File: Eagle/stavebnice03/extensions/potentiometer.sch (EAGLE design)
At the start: 4 parts

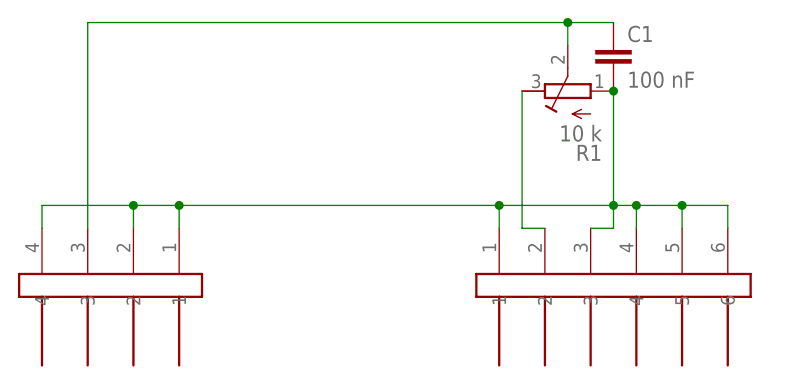
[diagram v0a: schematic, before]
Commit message: eagle adjustment for the Jíťa version
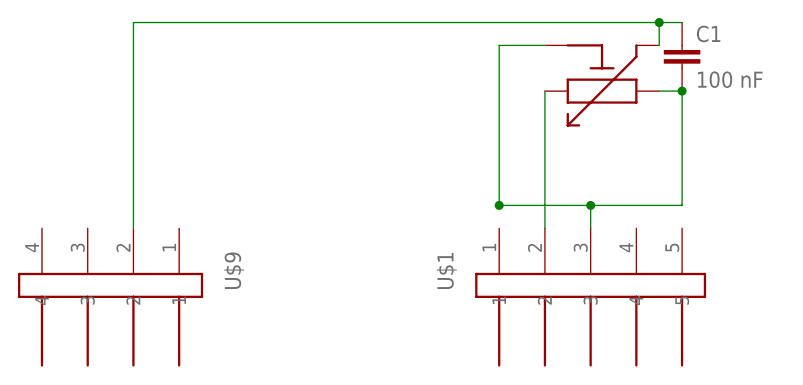
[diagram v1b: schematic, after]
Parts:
- removed R1: 10 k, !stavebnice03:R-TRIM
- removed U$8: JUMPER6M, !stavebnice03:JUMPER6M
- added U$1: JUMPER5M, !stavebnice03:JUMPER5M
- added U$2: POTENTIOMETER-RK09, !stavebnice03:POTENTIOMETER-RK09
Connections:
- net GND: now also U$1.3, U$2.1, U$2.GND; no longer R1.E, U$8.1, U$8.3, U$8.4, U$8.5, U$8.6, U$9.1, U$9.2, U$9.4
- net N$1: now also U$2.2, U$9.2; no longer R1.S, U$9.3
- net N$2: now also U$1.2, U$2.3; no longer R1.A, U$8.2
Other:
- moved on the sheet: C1
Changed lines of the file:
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@@
 </classes>
 <parts>
-<part name="U$8" library="!stavebnice03" deviceset="JUMPER6M" device=""/>
 <part name="U$9" library="!stavebnice03" deviceset="JUMPER4M" device=""/>
-<part name="R1" library="!stavebnice03" deviceset="R-TRIM" device="" value="10 k"/>
 <part name="C1" library="resistor" deviceset="C-EU" device="C0805" value="100 nF"/>
+<part name="U$1" library="!stavebnice03" deviceset="JUMPER5M" device=""/>
+<part name="U$2" library="!stavebnice03" deviceset="POTENTIOMETER-RK09" device=""/>
 </parts>
 <sheets>
@@
 </plain>
 <instances>
-<instance part="U$8" gate="G$1" x="175.26" y="35.56" rot="MR270"/>
 <instance part="U$9" gate="G$1" x="119.38" y="35.56" rot="R270"/>
-<instance part="R1" gate="G$1" x="170.18" y="58.42" rot="R90"/>
-<instance part="C1" gate="G$1" x="175.26" y="63.5"/>
+<instance part="C1" gate="G$1" x="182.88" y="63.5"/>
+<instance part="U$1" gate="G$1" x="172.72" y="35.56" rot="MR270"/>
+<instance part="U$2" gate="G$1" x="177.8" y="58.42" rot="R180"/>
 </instances>
 <busses>
@@
 <net name="N$1" class="0">
 <segment>
-<pinref part="U$9" gate="G$1" pin="3"/>
-<wire x1="116.84" y1="43.18" x2="116.84" y2="66.04" width="0.1524" layer="91"/>
-<wire x1="116.84" y1="66.04" x2="170.18" y2="66.04" width="0.1524" layer="91"/>
-<wire x1="170.18" y1="66.04" x2="170.18" y2="63.5" width="0.1524" layer="91"/>
-<pinref part="R1" gate="G$1" pin="S"/>
+<wire x1="121.92" y1="66.04" x2="180.34" y2="66.04" width="0.1524" layer="91"/>
+<wire x1="180.34" y1="66.04" x2="180.34" y2="63.5" width="0.1524" layer="91"/>
 <pinref part="C1" gate="G$1" pin="1"/>
-<wire x1="170.18" y1="66.04" x2="175.26" y2="66.04" width="0.1524" layer="91"/>
-<junction x="170.18" y="66.04"/>
+<wire x1="180.34" y1="66.04" x2="182.88" y2="66.04" width="0.1524" layer="91"/>
+<junction x="180.34" y="66.04"/>
+<pinref part="U$2" gate="G$1" pin="2"/>
+<pinref part="U$9" gate="G$1" pin="2"/>
+<wire x1="121.92" y1="66.04" x2="121.92" y2="43.18" width="0.1524" layer="91"/>
 </segment>
 </net>
 <net name="N$2" class="0">
 <segment>
-<pinref part="U$8" gate="G$1" pin="2"/>
-<wire x1="167.64" y1="43.18" x2="165.1" y2="43.18" width="0.1524" layer="91"/>
-<pinref part="R1" gate="G$1" pin="A"/>
-<wire x1="165.1" y1="43.18" x2="165.1" y2="58.42" width="0.1524" layer="91"/>
+<wire x1="167.64" y1="43.18" x2="167.64" y2="58.42" width="0.1524" layer="91"/>
+<pinref part="U$2" gate="G$1" pin="3"/>
+<pinref part="U$1" gate="G$1" pin="2"/>
 </segment>
 </net>
 <net name="GND" class="0">
 <segment>
-<pinref part="U$8" gate="G$1" pin="3"/>
-<pinref part="R1" gate="G$1" pin="E"/>
-<wire x1="175.26" y1="43.18" x2="175.26" y2="45.72" width="0.1524" layer="91"/>
-<wire x1="175.26" y1="45.72" x2="175.26" y2="58.42" width="0.1524" layer="91"/>
-<wire x1="175.26" y1="43.18" x2="172.72" y2="43.18" width="0.1524" layer="91"/>
+<wire x1="172.72" y1="43.18" x2="172.72" y2="45.72" width="0.1524" layer="91"/>
+<wire x1="182.88" y1="45.72" x2="182.88" y2="58.42" width="0.1524" layer="91"/>
 <pinref part="C1" gate="G$1" pin="2"/>
-<junction x="175.26" y="58.42"/>
-<pinref part="U$9" gate="G$1" pin="1"/>
-<wire x1="127" y1="43.18" x2="127" y2="45.72" width="0.1524" layer="91"/>
-<pinref part="U$9" gate="G$1" pin="2"/>
-<wire x1="121.92" y1="43.18" x2="121.92" y2="45.72" width="0.1524" layer="91"/>
-<wire x1="121.92" y1="45.72" x2="111.76" y2="45.72" width="0.1524" layer="91"/>
-<pinref part="U$9" gate="G$1" pin="4"/>
-<wire x1="111.76" y1="43.18" x2="111.76" y2="45.72" width="0.1524" layer="91"/>
-<wire x1="121.92" y1="45.72" x2="127" y2="45.72" width="0.1524" layer="91"/>
-<junction x="121.92" y="45.72"/>
-<junction x="127" y="45.72"/>
-<wire x1="127" y1="45.72" x2="162.56" y2="45.72" width="0.1524" layer="91"/>
-<junction x="175.26" y="45.72"/>
-<pinref part="U$8" gate="G$1" pin="1"/>
-<wire x1="162.56" y1="45.72" x2="175.26" y2="45.72" width="0.1524" layer="91"/>
-<wire x1="162.56" y1="43.18" x2="162.56" y2="45.72" width="0.1524" layer="91"/>
-<pinref part="U$8" gate="G$1" pin="4"/>
-<wire x1="177.8" y1="43.18" x2="177.8" y2="45.72" width="0.1524" layer="91"/>
-<wire x1="177.8" y1="45.72" x2="175.26" y2="45.72" width="0.1524" layer="91"/>
-<pinref part="U$8" gate="G$1" pin="5"/>
-<wire x1="182.88" y1="43.18" x2="182.88" y2="45.72" width="0.1524" layer="91"/>
-<wire x1="182.88" y1="45.72" x2="177.8" y2="45.72" width="0.1524" layer="91"/>
-<wire x1="182.88" y1="45.72" x2="187.96" y2="45.72" width="0.1524" layer="91"/>
-<pinref part="U$8" gate="G$1" pin="6"/>
-<wire x1="187.96" y1="45.72" x2="187.96" y2="43.18" width="0.1524" layer="91"/>
-<junction x="177.8" y="45.72"/>
+<wire x1="162.56" y1="45.72" x2="172.72" y2="45.72" width="0.1524" layer="91"/>
+<wire x1="172.72" y1="45.72" x2="182.88" y2="45.72" width="0.1524" layer="91"/>
 <junction x="162.56" y="45.72"/>
-<junction x="182.88" y="45.72"/>
+<pinref part="U$2" gate="G$1" pin="1"/>
+<junction x="172.72" y="45.72"/>
+<wire x1="180.34" y1="58.42" x2="182.88" y2="58.42" width="0.1524" layer="91"/>
+<pinref part="U$2" gate="G$1" pin="GND"/>
+<wire x1="167.64" y1="63.5" x2="162.56" y2="63.5" width="0.1524" layer="91"/>
+<wire x1="162.56" y1="63.5" x2="162.56" y2="45.72" width="0.1524" layer="91"/>
+<pinref part="U$1" gate="G$1" pin="3"/>
+<junction x="182.88" y="58.42"/>
 </segment>
 </net>
